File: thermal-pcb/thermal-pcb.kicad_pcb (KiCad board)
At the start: 2 copper layers, 10 parts, among them J1 RS/E pins, J2 Conn_01x16_Female, J3 Data and power pins, J4 Temp sensor pins

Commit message: Update PCB sheme.
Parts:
- added ARK: TerminalBlock_bornier-3_P5.08mm, TerminalBlock:TerminalBlock_bornier-3_P5.08mm, F.Cu at (175.5, 71.5)
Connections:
- 4.7k1 pad 1: (no net) -> Net-(4.7k1-Pad2)
- 4.7k1 pad 2: Net-(4.7k1-Pad2) -> +5V
- J4 pad 1: (no net) -> Net-(4.7k1-Pad2)
- J4 pad 2: (no net) -> Net-(4.7k1-Pad2)
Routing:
- net +5V: track 0.00 -> 160.0 mm, vias 0 -> 4
- net (no net): track 152.5 -> 0.00 mm, vias 5 -> 0
- net Net-(4.7k1-Pad2): track 0.00 -> 43.0 mm

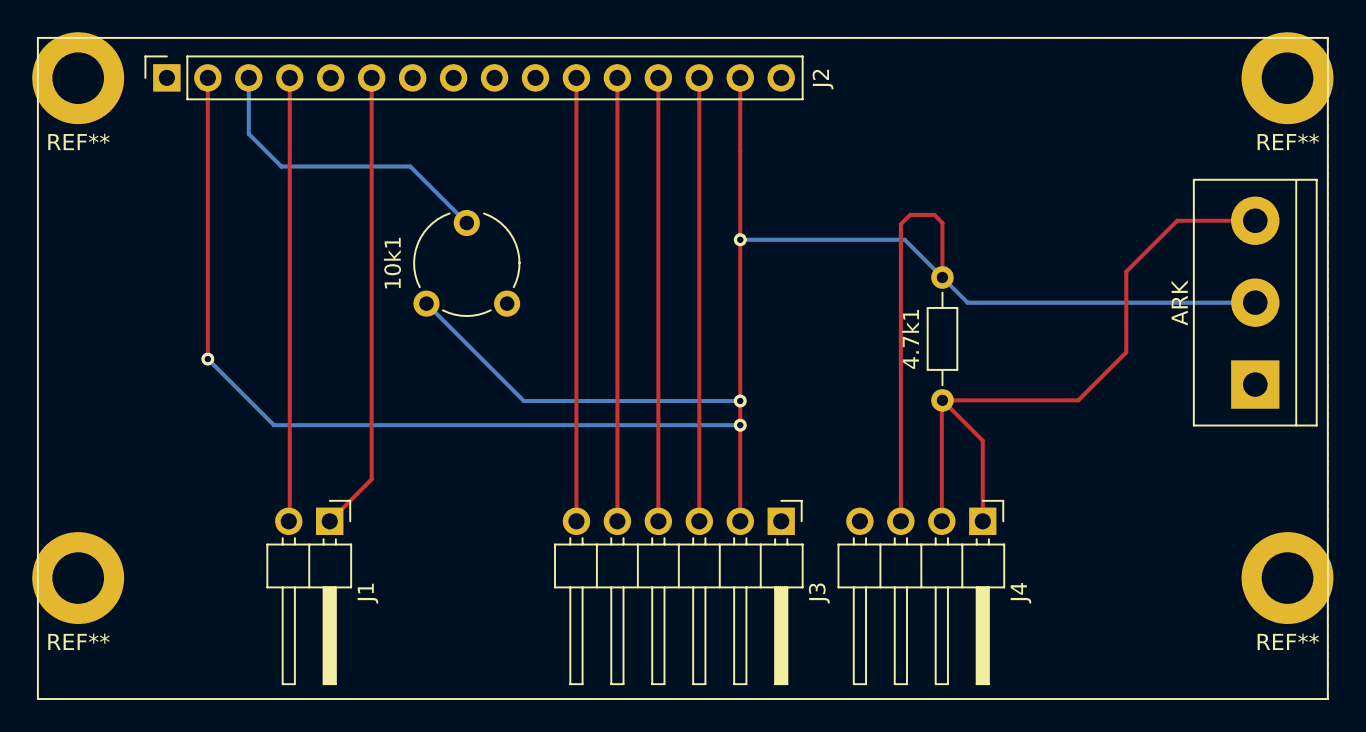
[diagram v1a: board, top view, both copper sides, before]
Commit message: PCB track width has been updated.
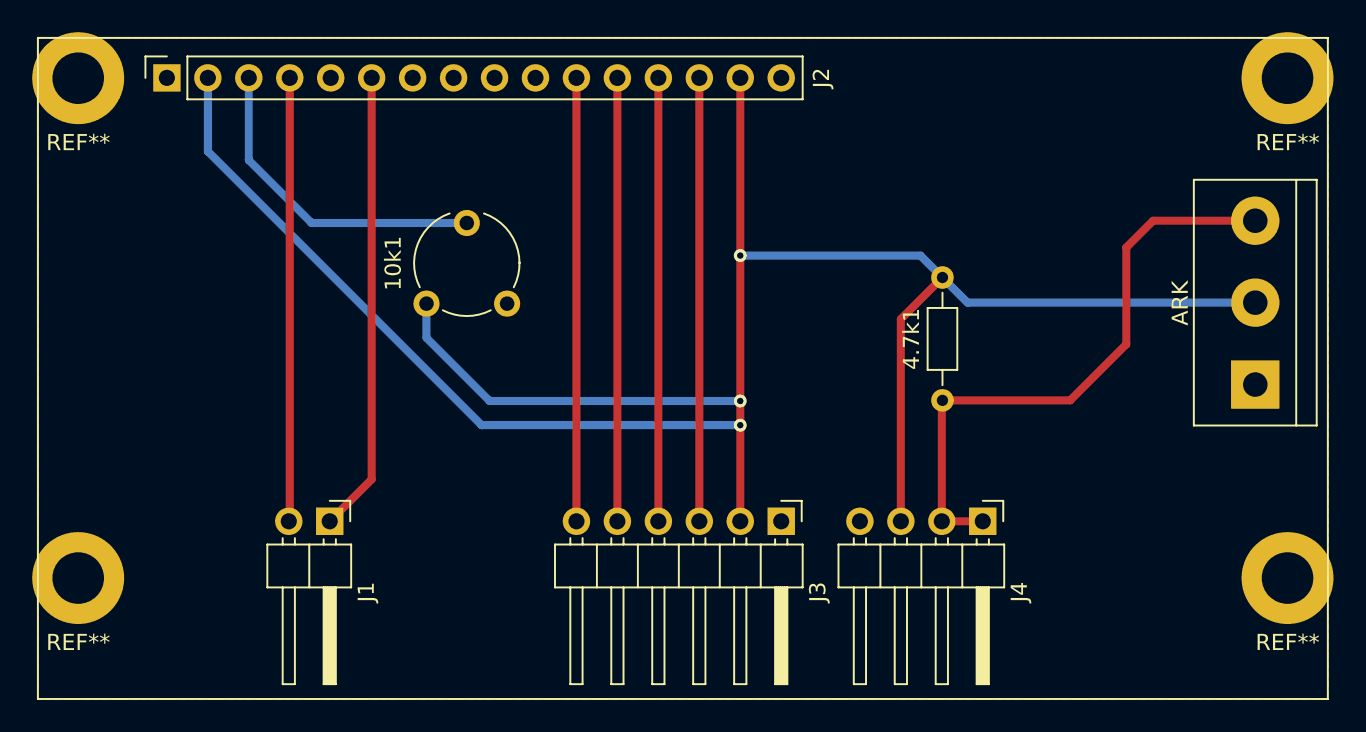
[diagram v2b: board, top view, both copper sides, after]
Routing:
- net +5V: track 160.0 -> 144.7 mm, vias 4 -> 3
- net Net-(4.7k1-Pad2): track 43.0 -> 37.6 mm
- net Net-(10k1-Pad2): track 19.3 -> 20.2 mm
